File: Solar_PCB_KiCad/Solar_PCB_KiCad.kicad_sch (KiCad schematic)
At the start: 22 parts, among them J1 Screw_Terminal_01x02, J2 Screw_Terminal_01x02, J3 Screw_Terminal_01x02, U1 LT3652EMSE

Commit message: Updated PCB Layout
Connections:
- no-connect marks 0 -> 1
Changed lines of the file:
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@@
 		(color 0 0 0 0)
+	)
+	(no_connect
+		(at 168.91 104.14)
 	)
 	(wire

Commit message: Updated PCB Layout
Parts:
- D4: footprint Diode_SMD:D_SMC -> Diode_SMD:D_SOD-323
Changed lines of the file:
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@@
+	)
+	(symbol
+		(lib_id "Device:D_Schottky")
+		(at 175.26 71.12 90)
+		(unit 1)
+		(exclude_from_sim no)
+		(in_bom yes)
+		(on_board yes)
+		(dnp no)
+		(property "Reference" "D4"
+			(at 173.99 74.676 0)
+			(effects
+				(font
+					(size 1.27 1.27)
+				)
+			)
+		)
+		(property "Value" "D_Schottky"
+			(at 171.958 70.866 0)
+			(effects
+				(font
+					(size 1.27 1.27)
+				)
+			)
+		)
+		(property "Footprint" "Diode_SMD:D_SOD-323"
+			(at 175.26 71.12 0)
+			(effects
+				(font
+					(size 1.27 1.27)
+				)
+				(hide yes)
+			)
+		)
+		(property "Datasheet" "https://www.mccsemi.com/pdf/Products/B5817WS-B5819WS(SOD-323).PDF"
+			(at 175.26 71.12 0)
+			(effects
+				(font
+					(size 1.27 1.27)
+				)
+				(hide yes)
+			)
+		)
+		(property "Description" "Schottky diode"
+			(at 175.26 71.12 0)
+			(effects
+				(font
+					(size 1.27 1.27)
+				)
+				(hide yes)
+			)
+		)
+		(pin "1"
+		)
+		(pin "2"
+		)
+		(instances
+			(project "Solar_PCB_KiCad"
+				(path "/6af0d19f-b029-4f07-94ac-1aca616d65fb"
+					(reference "D4")
+					(unit 1)
+				)
+			)
+		)
 	)
 	(symbol
@@
 					(unit 1)
 				)
-			)
-		)
-	)
-	(symbol
-		(lib_id "Device:D_Schottky")
-		(at 175.26 71.12 90)
-		(unit 1)
-		(exclude_from_sim no)
-		(in_bom yes)
-		(on_board yes)
-		(dnp no)
-		(fields_autoplaced yes)
-		(property "Reference" "D4"
-			(at 178.3771 70.1674 90)
-			(effects
-				(font
-					(size 1.27 1.27)
-				)
-				(justify right)
-			)
-		)
-		(property "Value" "D_Schottky"
-			(at 178.3771 72.7074 90)
-			(effects
-				(font
-					(size 1.27 1.27)
-				)
-				(justify right)
-			)
-		)
-		(property "Footprint" "Diode_SMD:D_SMC"
-			(at 175.26 71.12 0)
-			(effects
-				(font
-					(size 1.27 1.27)
-				)
-				(hide yes)
-			)
-		)
-		(property "Datasheet" "https://www.onsemi.com/pdf/datasheet/mbrs340t3-d.pdf"
-			(at 175.26 71.12 0)
-			(effects
-				(font
-					(size 1.27 1.27)
-				)
-				(hide yes)
-			)
-		)
-		(property "Description" "Schottky diode"
-			(at 175.26 71.12 0)
-			(effects
-				(font
-					(size 1.27 1.27)
-				)
-				(hide yes)
-			)
-		)
-		(pin "1"
-		)
-		(pin "2"
-		)
-		(instances
-			(project "Solar_PCB_KiCad"
-				(path "/6af0d19f-b029-4f07-94ac-1aca616d65fb"
-					(reference "D4")
-					(unit 1)
-				)

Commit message: Updated PCB Layout
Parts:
- D4: footprint Diode_SMD:D_SOD-323 -> Diode_SMD:D_SMC_Handsoldering
- L1: value 20uH -> 24uH; footprint Inductor_THT:L_Radial_D7.8mm_P5.00mm_Fastron_07HCP -> Inductor_SMD:L_Wuerth_WE-PDF_Handsoldering
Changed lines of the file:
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@@
 			)
 		)
-		(property "Footprint" "Diode_SMD:D_SOD-323"
+		(property "Footprint" "Diode_SMD:D_SMC_Handsoldering"
 			(at 175.26 71.12 0)
 			(effects
@@
 			)
 		)
-		(property "Value" "20uH"
+		(property "Value" "24uH"
 			(at 186.69 78.74 90)
 			(effects
@@
 			)
 		)
-		(property "Footprint" "Inductor_THT:L_Radial_D7.8mm_P5.00mm_Fastron_07HCP"
+		(property "Footprint" "Inductor_SMD:L_Wuerth_WE-PDF_Handsoldering"
 			(at 186.69 81.28 0)
 			(effects

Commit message: Updated Layout
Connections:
- net GND: now also J2.1 (Pin_1); no longer J2.2 (Pin_2)
- net at C1.1, D3.2 (A), J3.1 (Pin_1)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: now also J2.2 (Pin_2); no longer J2.1 (Pin_1)
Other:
- moved on the sheet: J2, J3
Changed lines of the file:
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@@
+	)
+	(junction
+		(at 212.09 81.28)
+		(diameter 0)
+		(color 0 0 0 0)
 	)
 	(junction
@@
 		(color 0 0 0 0)
 	)
-	(junction
-		(at 212.09 81.28)
-		(diameter 0)
-		(color 0 0 0 0)
-	)
 	(no_connect
 		(at 168.91 104.14)
@@
 	(wire
 		(pts
+			(xy 212.09 81.28) (xy 215.9 81.28)
+		)
+		(stroke
+			(width 0)
+			(type default)
+		)
+	)
+	(wire
+		(pts
 			(xy 101.6 87.63) (xy 101.6 88.9)
 		)
@@
 	(wire
 		(pts
+			(xy 241.3 81.28) (xy 241.3 77.47)
+		)
+		(stroke
+			(width 0)
+			(type default)
+		)
+	)
+	(wire
+		(pts
 			(xy 139.7 77.47) (xy 139.7 91.44)
 		)
@@
 	(wire
 		(pts
+			(xy 135.89 96.52) (xy 135.89 88.9)
+		)
+		(stroke
+			(width 0)
+			(type default)
+		)
+	)
+	(wire
+		(pts
+			(xy 129.54 67.31) (xy 129.54 64.77)
+		)
+		(stroke
+			(width 0)
+			(type default)
+		)
+	)
+	(wire
+		(pts
+			(xy 241.3 83.82) (xy 241.3 88.9)
+		)
+		(stroke
+			(width 0)
+			(type default)
+		)
+	)
+	(wire
+		(pts
 			(xy 212.09 83.82) (xy 212.09 88.9)
 		)
@@
 	(wire
 		(pts
-			(xy 135.89 96.52) (xy 135.89 88.9)
-		)
-		(stroke
-			(width 0)
-			(type default)
-		)
-	)
-	(wire
-		(pts
-			(xy 129.54 67.31) (xy 129.54 64.77)
-		)
-		(stroke
-			(width 0)
-			(type default)
-		)
-	)
-	(wire
-		(pts
 			(xy 139.7 91.44) (xy 143.51 91.44)
 		)
@@
 	(wire
 		(pts
+			(xy 241.3 81.28) (xy 246.38 81.28)
+		)
+		(stroke
+			(width 0)
+			(type default)
+		)
+	)
+	(wire
+		(pts
 			(xy 101.6 77.47) (xy 101.6 80.01)
 		)
@@
 	(wire
 		(pts
-			(xy 241.3 83.82) (xy 241.3 88.9)
-		)
-		(stroke
-			(width 0)
-			(type default)
-		)
-	)
-	(wire
-		(pts
 			(xy 204.47 81.28) (xy 201.93 81.28)
 		)
@@
 	(wire
 		(pts
-			(xy 241.3 77.47) (xy 241.3 81.28)
+			(xy 212.09 83.82) (xy 215.9 83.82)
 		)
 		(stroke
@@
 		(pts
 			(xy 198.12 116.84) (xy 198.12 119.38)
+		)
+		(stroke
+			(width 0)
+			(type default)
+		)
+	)
+	(wire
+		(pts
+			(xy 246.38 83.82) (xy 241.3 83.82)
 		)
 		(stroke
@@
 	(symbol
 		(lib_id "Connector:Screw_Terminal_01x02")
-		(at 246.38 81.28 0)
+		(at 220.98 81.28 0)
 		(unit 1)
 		(exclude_from_sim no)
@@
 		(dnp no)
 		(property "Reference" "J3"
-			(at 249.174 84.074 0)
+			(at 223.774 84.074 0)
 			(effects
 				(font
@@
 		)
 		(property "Value" "Screw_Terminal_01x02"
-			(at 258.826 81.28 0)
+			(at 233.426 81.28 0)
 			(effects
 				(font
@@
 		)
 		(property "Footprint" "TerminalBlock_Phoenix:TerminalBlock_Phoenix_MKDS-1,5-2-5.08_1x02_P5.08mm_Horizontal"
-			(at 246.38 81.28 0)
+			(at 220.98 81.28 0)
 			(effects
 				(font
@@
 		)
 		(property "Datasheet" "~"
-			(at 246.38 81.28 0)
+			(at 220.98 81.28 0)
 			(effects
 				(font
@@
 		)
 		(property "Description" "Generic screw terminal, single row, 01x02, script generated (kicad-library-utils/schlib/autogen/connector/)"
-			(at 246.38 81.28 0)
+			(at 220.98 81.28 0)
 			(effects
 				(font
@@
 	(symbol
 		(lib_id "Connector:Screw_Terminal_01x02")
-		(at 217.17 81.28 0)
+		(at 251.46 83.82 0)
+		(mirror x)
 		(unit 1)
 		(exclude_from_sim no)
@@
 		(dnp no)
 		(property "Reference" "J2"
-			(at 219.964 84.074 0)
+			(at 254.254 81.026 0)
 			(effects
 				(font
@@
 		)
 		(property "Value" "Screw_Terminal_01x02"
-			(at 229.616 81.28 0)
+			(at 263.906 83.82 0)
 			(effects
 				(font
@@
 		)
 		(property "Footprint" "TerminalBlock_Phoenix:TerminalBlock_Phoenix_MKDS-1,5-2-5.08_1x02_P5.08mm_Horizontal"
-			(at 217.17 81.28 0)
+			(at 251.46 83.82 0)
 			(effects
 				(font
@@
 		)
 		(property "Datasheet" "~"
-			(at 217.17 81.28 0)
+			(at 251.46 83.82 0)
 			(effects
 				(font
@@
 		)
 		(property "Description" "Generic screw terminal, single row, 01x02, script generated (kicad-library-utils/schlib/autogen/connector/)"
-			(at 217.17 81.28 0)
-			(effects
-				(font
+			(at 251.46 83.82 0)
+			(effects
+				(font

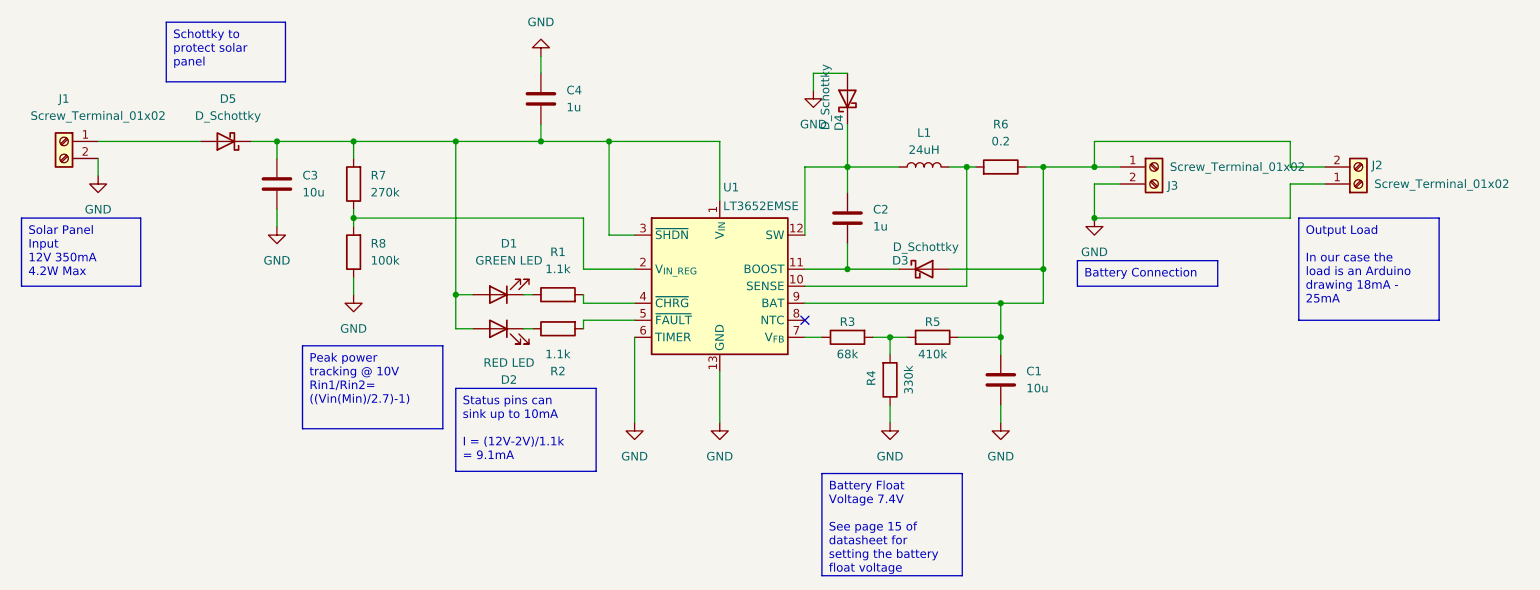
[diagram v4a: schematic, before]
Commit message: Added optional bypass and input capacitance
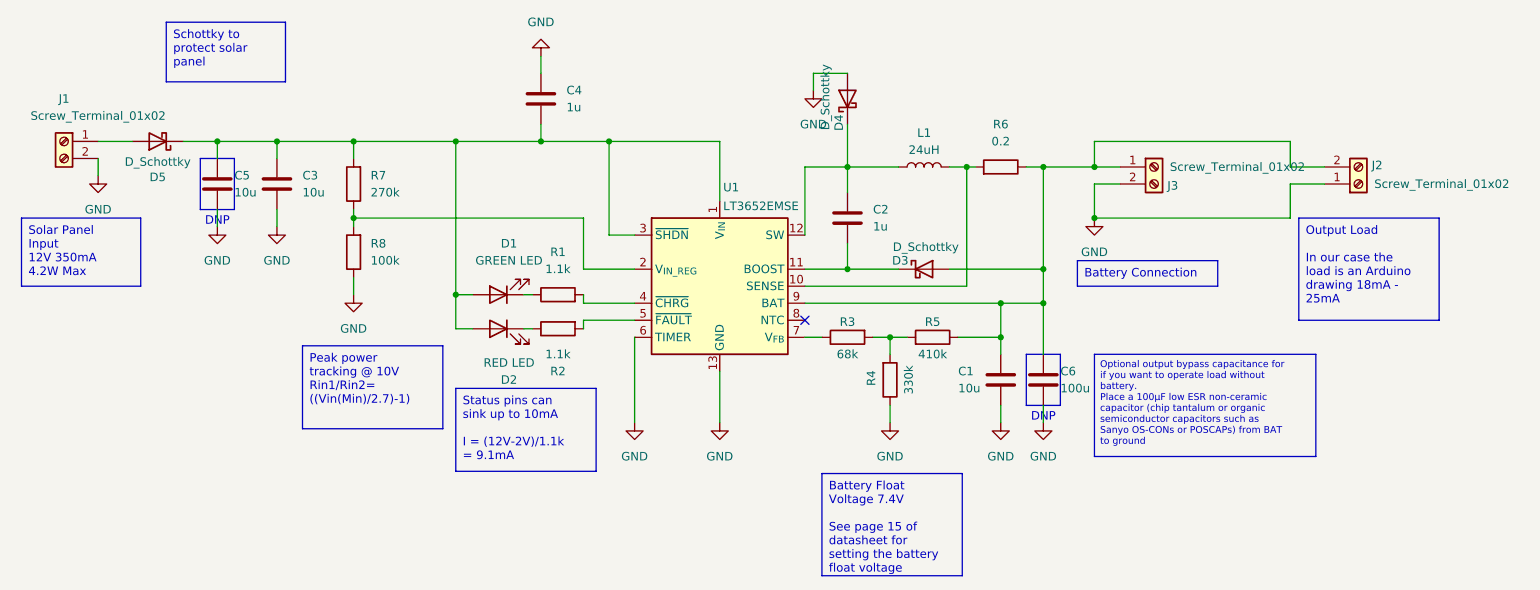
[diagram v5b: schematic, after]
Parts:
- added C5: 10u, Capacitor_SMD:C_0603_1608Metric, symbol Device:C
- added C6: 100u, Capacitor_SMD:C_0603_1608Metric, symbol Device:C
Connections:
- net GND: now also C5.2, C6.2
- net at C3.1, C4.1, D1.2 (A)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: now also C5.1
- net at C1.1, D3.2 (A), J2.2 (Pin_2)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: now also C6.1
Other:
- note added: "DNP"
- moved on the sheet: D5

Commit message: Updated diode + render + thermal considerations
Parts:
- D5: footprint Diode_SMD:D_SOD-323 -> Diode_SMD:D_SMP_DO-220AA
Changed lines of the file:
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@@
 			)
 		)
-		(property "Footprint" "Diode_SMD:D_SOD-323"
+		(property "Footprint" "Diode_SMD:D_SMP_DO-220AA"
 			(at 72.39 77.47 0)
 			(effects
@@
 			)
 		)
-		(property "Datasheet" "https://www.mccsemi.com/pdf/Products/B5817WS-B5819WS(SOD-323).PDF"
+		(property "Datasheet" "https://www.vishay.com/docs/88910/ss2p2.pdf"
 			(at 72.39 77.47 0)
 			(effects

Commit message: Updated output files
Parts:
- R6: value 0.2 -> 0.25
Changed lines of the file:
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@@
 			)
 		)
-		(property "Value" "0.2"
+		(property "Value" "0.25"
 			(at 198.12 77.47 90)
 			(effects
